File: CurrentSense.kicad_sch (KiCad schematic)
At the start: 20 parts, among them J4 I2C_5V

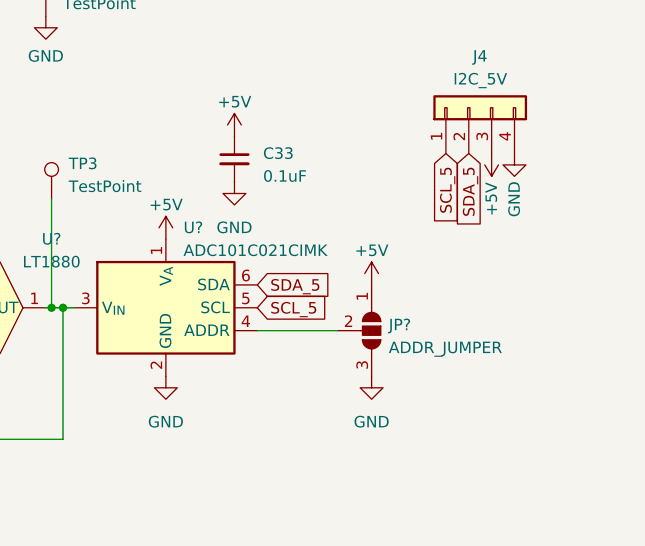
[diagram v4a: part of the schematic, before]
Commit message: Updated with selectable I2C addresses
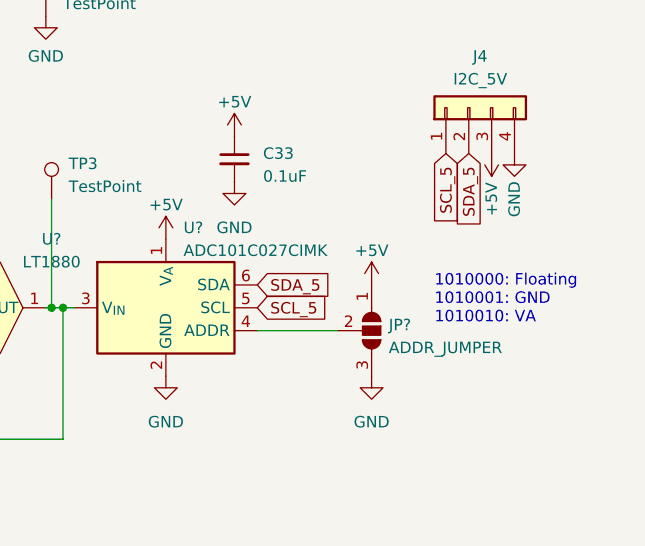
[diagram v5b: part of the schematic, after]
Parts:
- U?: value ADC101C021CIMK -> ADC101C027CIMK
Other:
- note added: "1010000: Floating 1010001: GND 1010010: VA"
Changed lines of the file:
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@@
     (stroke (width 0) (type default))
+  )
+  (text "1010000: Floating\n1010001: GND\n1010010: VA" (at 212.09 73.025 0)
+    (effects (font (size 1.27 1.27)) (justify left bottom))
   )
   (text "Prefer low-leakage\nfilm caps" (at 119.38 66.675 90)
@@
       (effects (font (size 1.27 1.27)) (justify left))
     )
-    (property "Value" "ADC101C021CIMK" (at 184.2009 64.77 0)
-      (effects (font (size 1.27 1.27)) (justify left))
-    )
+    (property "Value" "ADC101C027CIMK" (at 184.2009 64.77 0)
+      (effects (font (size 1.27 1.27)) (justify left))
+    )
